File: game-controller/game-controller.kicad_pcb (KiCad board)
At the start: 2 copper layers, 116.8 x 78.7 mm, 20 parts, among them J1 Conn_01x22, J10 Conn_01x01, J11 Conn_01x01, J12 Conn_01x01, J13 Conn_01x01, J14 Conn_01x01, J15 Conn_01x01, J16 Conn_01x01, J2 Conn_01x22, J3 Conn_01x01, J4 Conn_01x01, J5 Conn_01x01, J6 Conn_01x01, J7 Conn_01x01, J8 Conn_01x01, J9 Conn_01x01

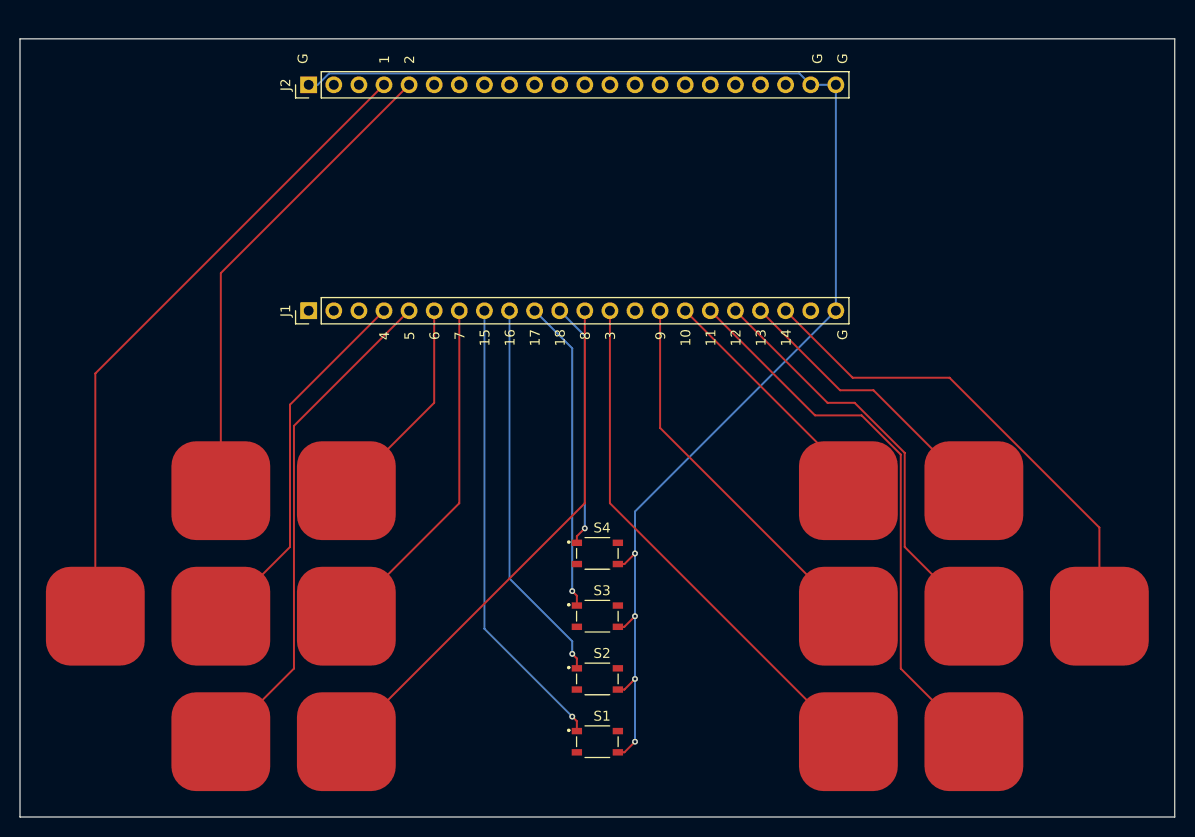
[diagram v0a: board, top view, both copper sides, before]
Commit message: Fix position of touch pads
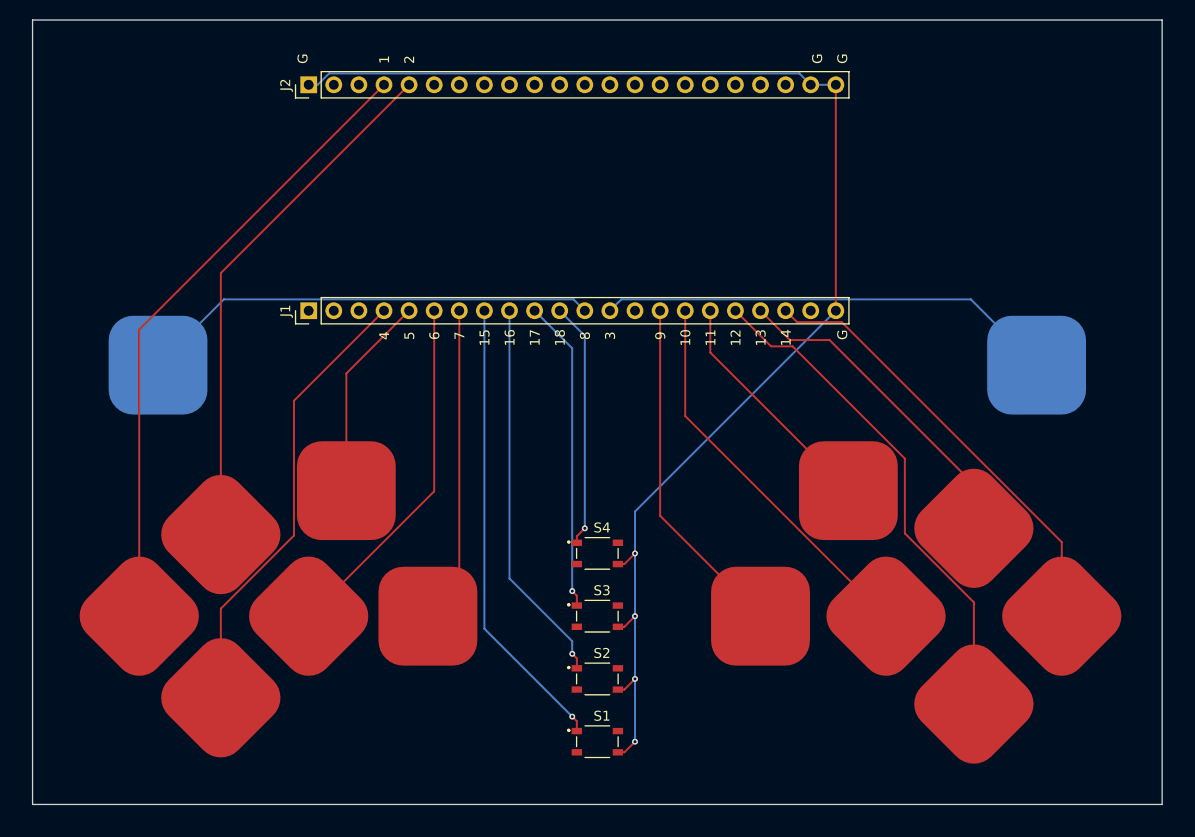
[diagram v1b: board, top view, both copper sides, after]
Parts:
- J10, J5: moved to B.Cu
- moved J10 42.6 mm to (108.0, 88.9), turned to 180 degrees
- moved J5 42.6 mm to (196.8, 88.9), turned to 180 degrees
- moved J7 28.4 mm to (127.0, 101.6)
- moved J13 28.4 mm to (177.8, 101.6)
- moved J12 13.3 mm to (181.6, 114.3), turned to 45 degrees
- moved J8 13.3 mm to (123.2, 114.3), turned to 45 degrees
- moved J11 8.89 mm to (168.9, 114.3)
- moved J14 8.89 mm to (190.5, 123.2), turned to 45 degrees
- moved J6 8.26 mm to (114.3, 122.6), turned to 45 degrees
- moved J9 8.25 mm to (135.3, 114.3)
- moved J3 4.45 mm to (106.0, 114.3), turned to 45 degrees
- moved J4 4.45 mm to (114.3, 106.0), turned to 45 degrees
- moved J15 3.81 mm to (199.4, 114.3), turned to 45 degrees
- moved J16 3.81 mm to (190.5, 105.4), turned to 45 degrees
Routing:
- net TOUCH11: track 57.4 -> 24.0 mm
- net TOUCH5: track 51.5 -> 20.8 mm
- net TOUCH10: track 25.0 -> 39.4 mm
- net TOUCH6: track 21.9 -> 36.2 mm
- net TOUCH12: track 42.5 -> 51.1 mm
- net TOUCH4: track 37.7 -> 46.0 mm
- net TOUCH8: track 53.6 -> 46.4 mm
- net TOUCH3: track 53.6 -> 46.4 mm
- net TOUCH14: track 49.8 -> 45.1 mm
- net TOUCH2: track 49.0 -> 53.4 mm
- net TOUCH13: track 29.1 -> 33.3 mm
- net TOUCH9: track 38.8 -> 35.1 mm
- net TOUCH7: track 35.6 -> 32.2 mm
- net TOUCH1: track 65.9 -> 64.0 mm
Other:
- board size 116.8 x 78.7 mm -> 114.3 x 79.4 mm

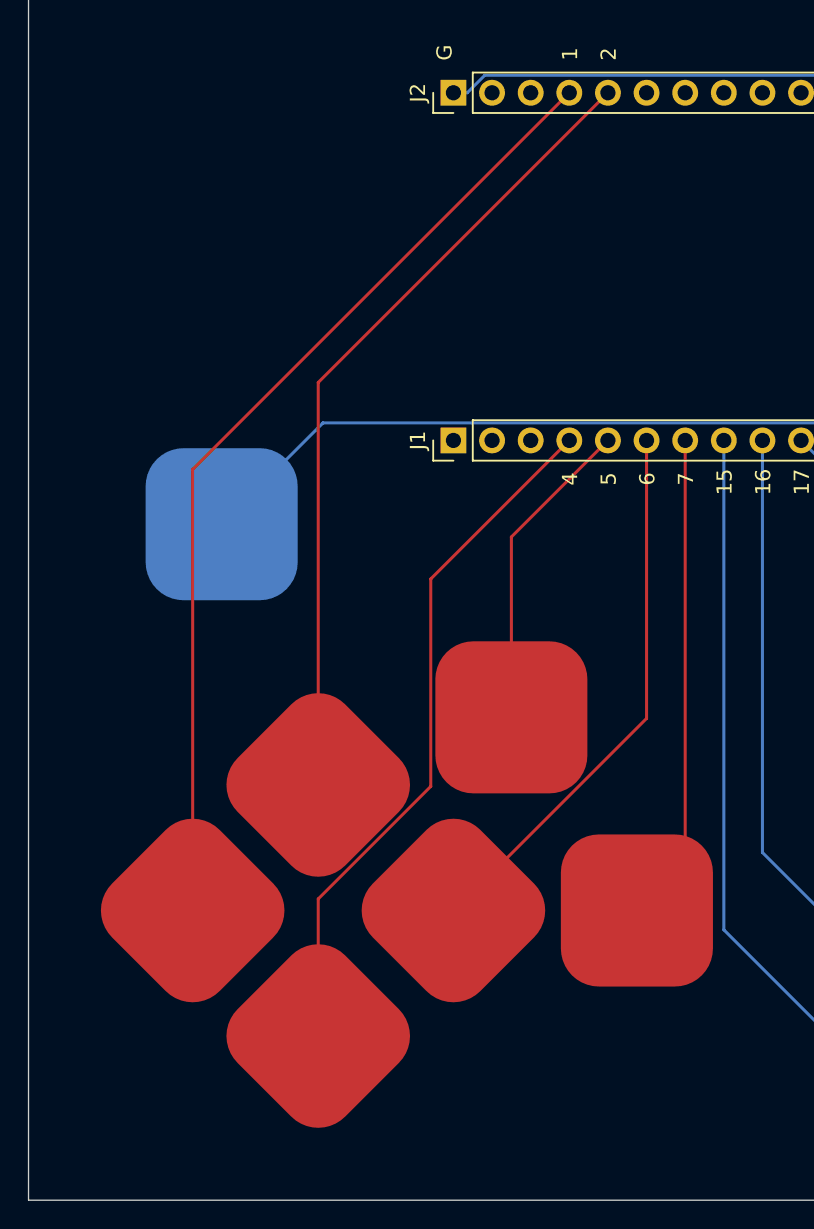
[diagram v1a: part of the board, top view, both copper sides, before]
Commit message: Fix touch position mistakes
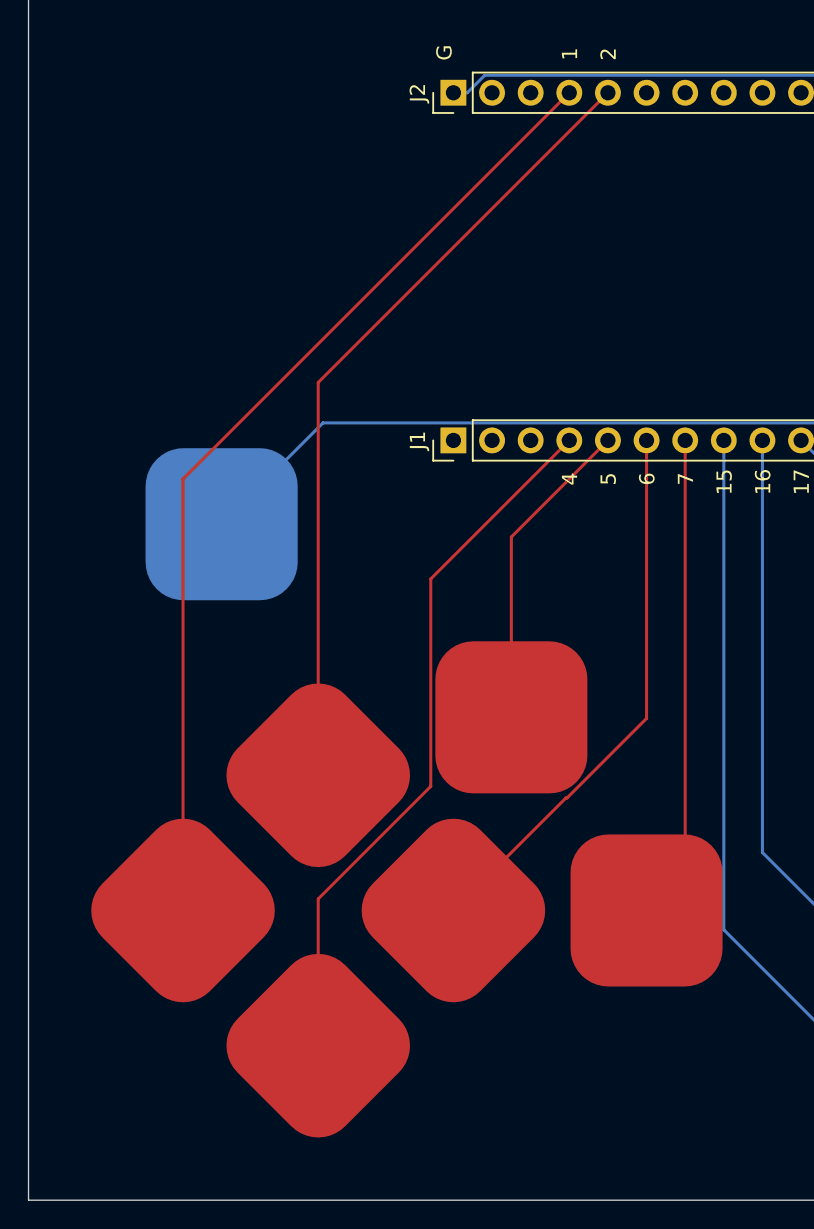
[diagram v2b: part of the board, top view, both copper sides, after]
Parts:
- moved J3 0.64 mm to (105.4, 114.3)
- moved J4 0.64 mm to (114.3, 105.4)
- moved J6 0.63 mm to (114.3, 123.2)
- moved J9 0.63 mm to (135.9, 114.3)
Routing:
- net TOUCH2: track 53.4 -> 52.8 mm
- net TOUCH4: track 46.0 -> 46.6 mm
- net TOUCH7: track 32.2 -> 31.7 mm
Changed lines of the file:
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@@
 	(footprint "Pad-CapacitiveTouch:Pad-CapacitiveTouch"
 		(layer "F.Cu")
-		(at 114.3 122.555 45)
+		(at 114.3 123.19 45)
 		(descr "<h3>Conductive Button</h3>\n<p>Used with rubber key pads on the <a href=\"https://www.sparkfun.com/products/retired/8602\">Nordic Key FOB</a>. This one was designed and proven to work with the <a href=\"https://www.sparkfun.com/products/retired/9377\">PolyCase Key FOB enclosures</a>.</p>")
 		(tags "SparkFun")
@@
 	(footprint "Pad-CapacitiveTouch:Pad-CapacitiveTouch"
 		(layer "F.Cu")
-		(at 106.045 114.3 45)
+		(at 105.41 114.3 45)
 		(descr "<h3>Conductive Button</h3>\n<p>Used with rubber key pads on the <a href=\"https://www.sparkfun.com/products/retired/8602\">Nordic Key FOB</a>. This one was designed and proven to work with the <a href=\"https://www.sparkfun.com/products/retired/9377\">PolyCase Key FOB enclosures</a>.</p>")
 		(tags "SparkFun")
@@
 	(footprint "Pad-CapacitiveTouch:Pad-CapacitiveTouch"
 		(layer "F.Cu")
-		(at 114.3 106.045 45)
+		(at 114.3 105.41 45)
 		(descr "<h3>Conductive Button</h3>\n<p>Used with rubber key pads on the <a href=\"https://www.sparkfun.com/products/retired/8602\">Nordic Key FOB</a>. This one was designed and proven to work with the <a href=\"https://www.sparkfun.com/products/retired/9377\">PolyCase Key FOB enclosures</a>.</p>")
 		(tags "SparkFun")
@@
 	(footprint "Pad-CapacitiveTouch:Pad-CapacitiveTouch"
 		(layer "F.Cu")
-		(at 135.255 114.3)
+		(at 135.89 114.3)
 		(descr "<h3>Conductive Button</h3>\n<p>Used with rubber key pads on the <a href=\"https://www.sparkfun.com/products/retired/8602\">Nordic Key FOB</a>. This one was designed and proven to work with the <a href=\"https://www.sparkfun.com/products/retired/9377\">PolyCase Key FOB enclosures</a>.</p>")
 		(tags "SparkFun")
@@
 	)
 	(segment
+		(start 121.7 92.5)
+		(end 130.81 83.39)
+		(width 0.2)
+		(layer "F.Cu")
+		(net 3)
+	)
+	(segment
+		(start 114.3 123.19)
+		(end 114.3 113.540334)
+		(width 0.2)
+		(layer "F.Cu")
+		(net 3)
+	)
+	(segment
+		(start 114.3 113.540334)
+		(end 121.7 106.140334)
+		(width 0.2)
+		(layer "F.Cu")
+		(net 3)
+	)
+	(segment
 		(start 121.7 106.140334)
 		(end 121.7 92.5)
@@
 	)
 	(segment
-		(start 114.3 113.540334)
-		(end 121.7 106.140334)
-		(width 0.2)
-		(layer "F.Cu")
-		(net 3)
-	)
-	(segment
-		(start 114.3 122.555)
-		(end 114.3 113.540334)
-		(width 0.2)
-		(layer "F.Cu")
-		(net 3)
-	)
-	(segment
-		(start 121.7 92.5)
-		(end 130.81 83.39)
-		(width 0.2)
-		(layer "F.Cu")
-		(net 3)
-	)
-	(segment
 		(start 158.75 104.14)
 		(end 158.75 83.39)
@@
 	)
 	(segment
-		(start 135.255 114.3)
-		(end 138.43 111.125)
+		(start 138.43 112.395)
+		(end 138.43 83.39)
 		(width 0.2)
 		(layer "F.Cu")
@@
 	)
 	(segment
-		(start 138.43 111.125)
-		(end 138.43 83.39)
+		(start 136.525 114.3)
+		(end 138.43 112.395)
 		(width 0.2)
 		(layer "F.Cu")
@@
 	)
 	(segment
-		(start 123.19 114.3)
-		(end 123.2598 114.3)
+		(start 130.6598 106.9)
+		(end 135.89 101.6698)
 		(width 0.2)
 		(layer "F.Cu")
@@
 	)
 	(segment
-		(start 123.2598 114.3)
-		(end 135.89 101.6698)
+		(start 130.59 106.9)
+		(end 130.6598 106.9)
 		(width 0.2)
 		(layer "F.Cu")
@@
 		(start 135.89 101.6698)
 		(end 135.89 83.39)
+		(width 0.2)
+		(layer "F.Cu")
+		(net 17)
+	)
+	(segment
+		(start 123.19 114.3)
+		(end 130.59 106.9)
 		(width 0.2)
 		(layer "F.Cu")
@@
 	)
 	(segment
-		(start 106.045 85.295)
+		(start 105.41 114.3)
+		(end 105.41 85.93)
+		(width 0.2)
+		(layer "F.Cu")
+		(net 32)
+	)
+	(segment
+		(start 105.41 85.93)
 		(end 130.81 60.53)
-		(width 0.2)
-		(layer "F.Cu")
-		(net 32)
-	)
-	(segment
-		(start 106.045 114.3)
-		(end 106.045 85.295)
 		(width 0.2)
 		(layer "F.Cu")
@@
 	)
 	(segment
-		(start 114.3 106.045)
+		(start 114.3 105.41)
 		(end 114.3 79.58)
 		(width 0.2)

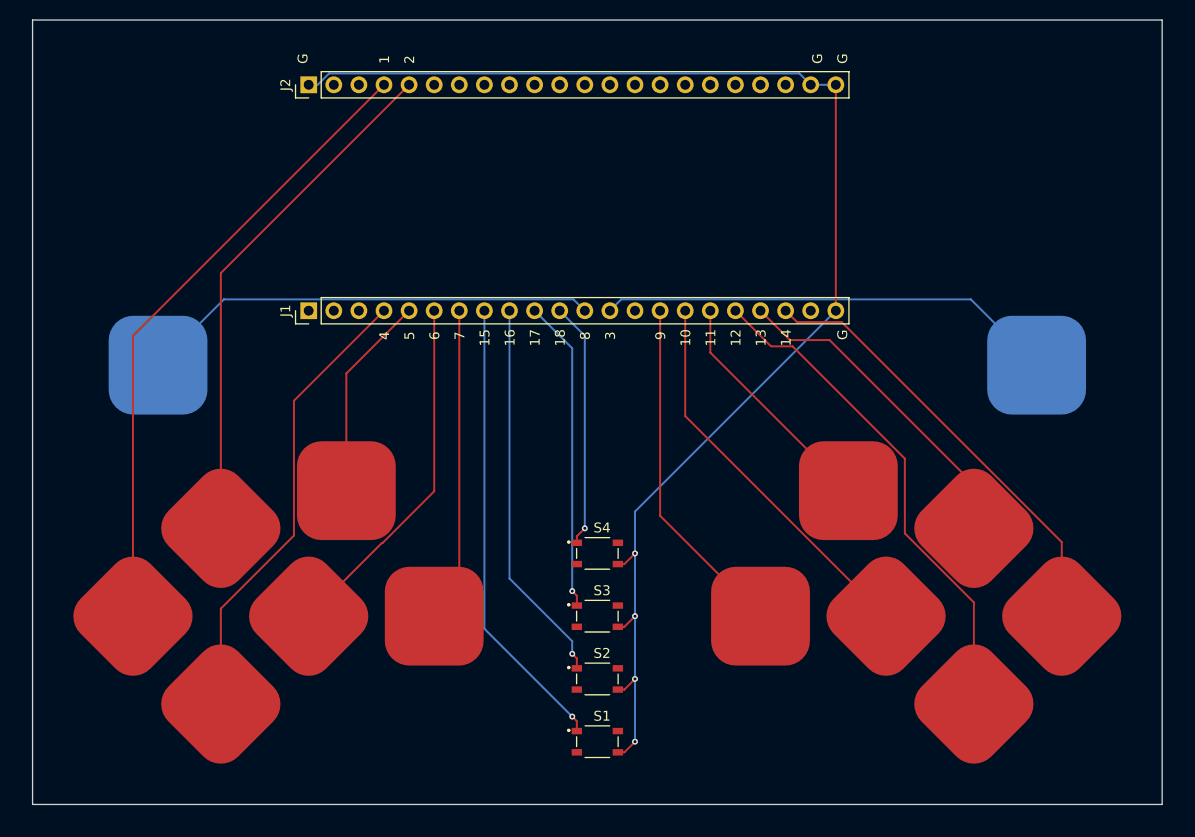
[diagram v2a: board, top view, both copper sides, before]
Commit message: Change PCB size of game-controller because of fablication price
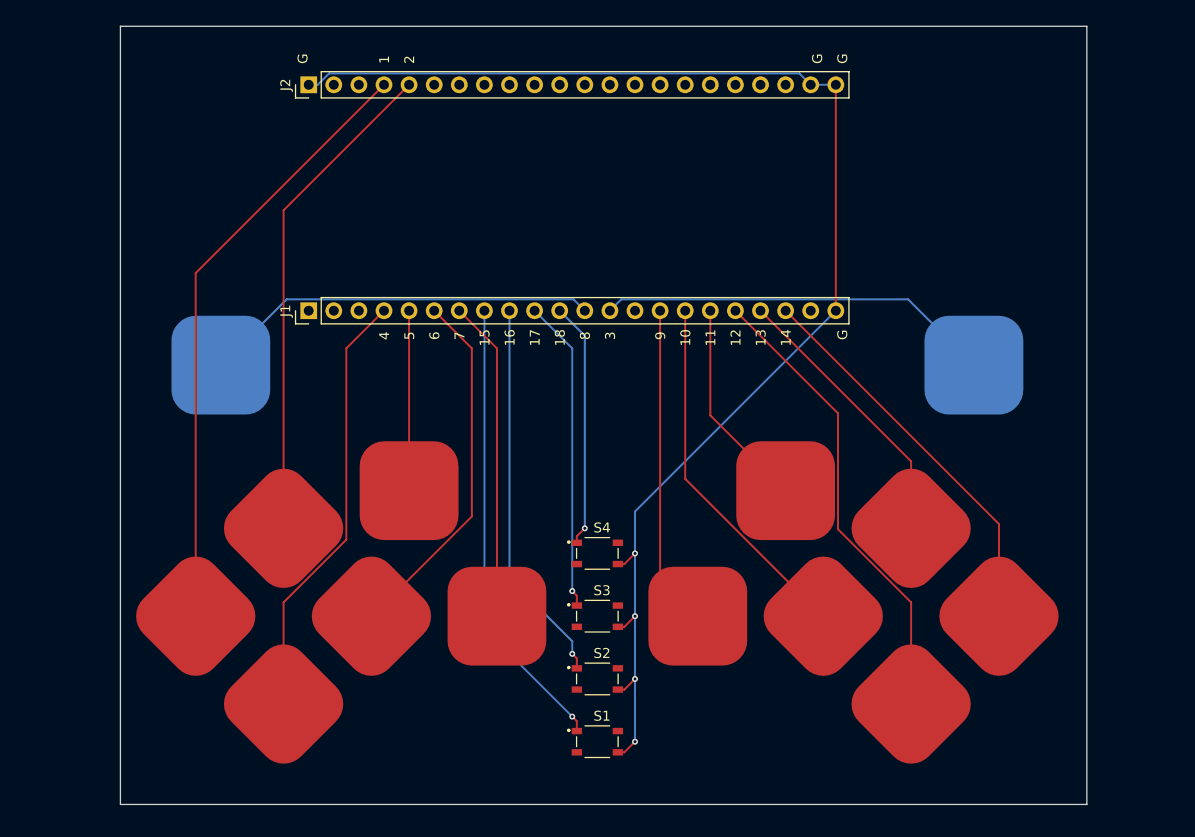
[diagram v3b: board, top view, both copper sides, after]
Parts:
- moved J12 6.35 mm to (175.3, 114.3)
- moved J13 6.35 mm to (171.4, 101.6)
- moved J9 6.35 mm to (142.2, 114.3)
- moved J3 6.35 mm to (111.8, 114.3)
- moved J4 6.35 mm to (120.7, 105.4)
- moved J6 6.35 mm to (120.7, 123.2)
- moved J10 6.35 mm to (114.3, 88.9)
- moved J11 6.35 mm to (162.6, 114.3)
- moved J14 6.35 mm to (184.2, 123.2)
- moved J15 6.35 mm to (193.0, 114.3)
- moved J16 6.35 mm to (184.2, 105.4)
- moved J5 6.35 mm to (190.5, 88.9)
- moved J7 6.35 mm to (133.3, 101.6)
- moved J8 6.35 mm to (129.5, 114.3)
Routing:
- net TOUCH8: track 46.4 -> 40.1 mm
- net TOUCH3: track 46.4 -> 40.1 mm
- net TOUCH14: track 45.1 -> 39.9 mm
- net TOUCH13: track 33.3 -> 28.3 mm
- net TOUCH12: track 51.1 -> 47.2 mm
- net TOUCH10: track 39.4 -> 36.7 mm
- net TOUCH11: track 24.0 -> 21.4 mm
- net TOUCH1: track 64.3 -> 61.7 mm
- net TOUCH4: track 46.6 -> 44.0 mm
- net TOUCH2: track 52.8 -> 50.1 mm
- net TOUCH9: track 35.1 -> 32.5 mm
- net TOUCH5: track 20.8 -> 18.2 mm
- net TOUCH7: track 31.7 -> 32.5 mm
- net TOUCH6: track 36.2 -> 36.7 mm
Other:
- board size 114.3 x 79.4 mm -> 97.8 x 78.7 mm
